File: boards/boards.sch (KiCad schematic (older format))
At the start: 3 parts

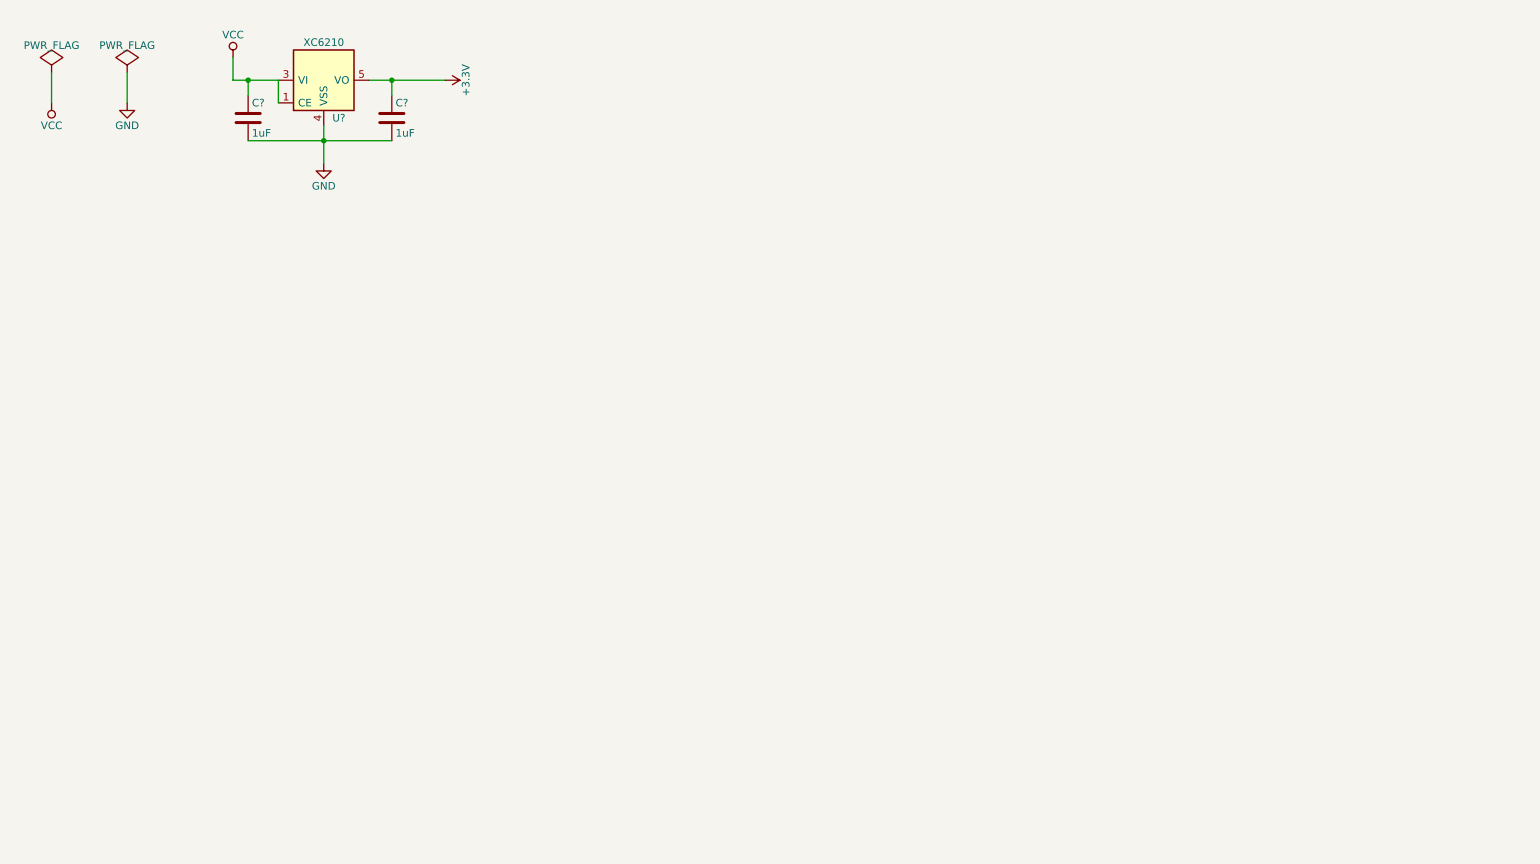
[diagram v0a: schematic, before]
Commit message: Schematics completed (rev 1). PCB layout started.
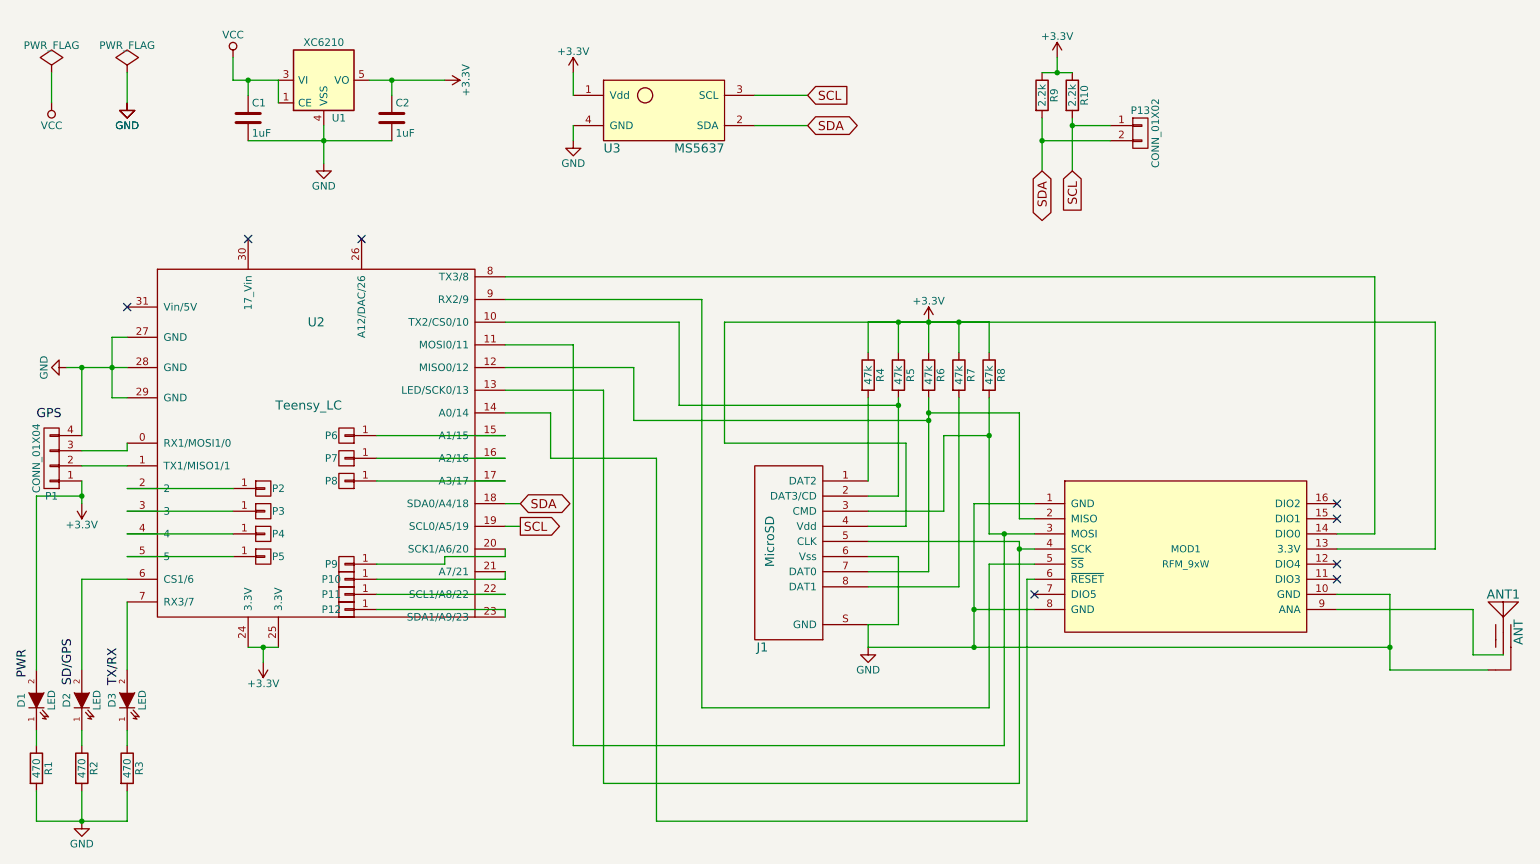
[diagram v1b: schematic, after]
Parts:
- added ANT1: ANT, Parts:ANT_50ohm, symbol ANT
- added D1: LED, william-parts:KPH-1608SGC, symbol LED
- added D2, D3: LED, william-parts:KingbrightKPTL-3216QBC-D-01, symbol LED
- added J1: MicroSD, Parts:DM3CS-SF, symbol MicroSD
- added MOD1: RFM_9xW, Parts:RFM9xW, symbol RFM_9xW
- added P1: CONN_01X04, william-parts:quadruple_pads, symbol CONN_01X04
- added P10, P11, P12, P2, P3, P4, P5, P6, P7, P8, P9: (no value), william-parts:single_pad, symbol CONN_01X01
- added P13: CONN_01X02, william-parts:double_pads, symbol CONN_01X02
- added R1, R2, R3: 470, Resistors_SMD.pretty:R_0805_HandSoldering, symbol R
- added R10, R9: 2.2k, Resistors_SMD.pretty:R_0805_HandSoldering, symbol R
- added R4, R5, R6, R7, R8: 47k, Resistors_SMD.pretty:R_0805_HandSoldering, symbol R
- added U2: Teensy_LC, william-parts:Teensy-LC, symbol Teensy_LC
- added U3: MS5637, Parts:MS5637, symbol MS5637
- C1, C2: renamed from C?; footprint (none) -> Capacitors_SMD.pretty:C_0805_HandSoldering
- U1: renamed from U?; footprint (none) -> TO_SOT_Packages_SMD.pretty:SOT-23-5
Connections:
- net +3V3: now also D1.2 (A), J1.4 (Vdd), MOD1.13 (3.3V), P1.1 (P1), R10.1, R4.1, R5.1, R6.1, R7.1, R8.1, R9.1, U2.24 (3.3V), U2.25 (3.3V), U3.1 (Vdd)
- net GND: now also ANT1.2, J1.6 (Vss), J1.S (GND), MOD1.1 (GND), MOD1.10 (GND), MOD1.8 (GND), P1.4 (P4), R1.2, R2.2, R3.2, U2.27 (GND), U2.28 (GND), U2.29 (GND), U3.4 (GND)
- new net: J1.1 (DAT2), R4.2
- new net: J1.2 (DAT3/CD), R5.2, U2.10 (TX2/CS0/10)
- new net: J1.3 (CMD), MOD1.3 (MOSI), R8.2, U2.11 (MOSI0/11)
- new net: J1.5 (CLK), MOD1.4 (SCK), U2.13 (LED/SCK0/13)
- new net: J1.7 (DAT0), MOD1.2 (MISO), R6.2, U2.12 (MISO0/12)
- new net: J1.8 (DAT1), R7.2
- new net: P1.3 (P3), U2.0 (RX1/MOSI1/0)
- new net: P1.2 (P2), U2.1 (TX1/MISO1/1)
- new net: MOD1.6 (~RESET), U2.14 (A0/14)
- new net: P6.1 (P1), U2.15 (A1/15)
- new net: P7.1 (P1), U2.16 (A2/16)
- new net: P8.1 (P1), U2.17 (A3/17)
- new net: P2.1 (P1), U2.2
- new net: P9.1 (P1), U2.20 (SCK1/A6/20)
- new net: P10.1 (P1), U2.21 (A7/21)
- new net: P11.1 (P1), U2.22 (SCL1/A8/22)
- new net: P12.1 (P1), U2.23 (SDA1/A9/23)
- new net: P3.1 (P1), U2.3
- new net: P4.1 (P1), U2.4
- new net: P5.1 (P1), U2.5
- new net: D2.2 (A), U2.6 (CS1/6)
- new net: D3.2 (A), U2.7 (RX3/7)
- new net: MOD1.14 (DIO0), U2.8 (TX3/8)
- new net: MOD1.5 (~SS), U2.9 (RX2/9)
- new net: ANT1.1, MOD1.9 (ANA)
- new net: D1.1 (K), R1.1
- new net: D2.1 (K), R2.1
- new net: D3.1 (K), R3.1
- new net SCL: P13.1 (P1), R10.2, U2.19 (SCL0/A5/19), U3.3 (SCL)
- new net SDA: P13.2 (P2), R9.2, U2.18 (SDA0/A4/18), U3.2 (SDA)
- no-connect marks 0 -> 8

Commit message: Changed to TO252 power reg. Continued trace connection.
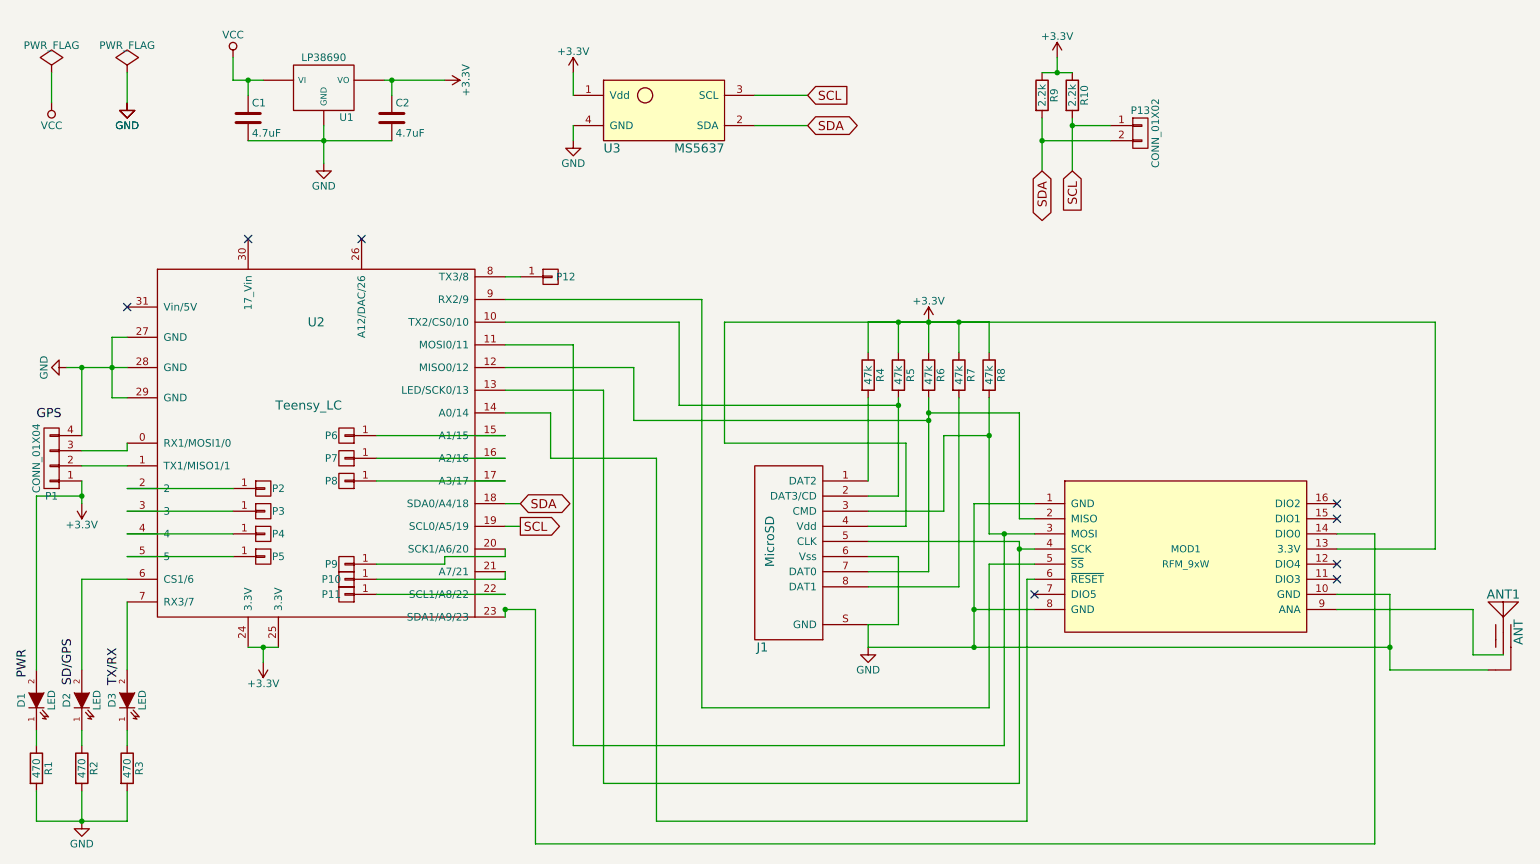
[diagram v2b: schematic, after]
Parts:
- removed U1: XC6210, TO_SOT_Packages_SMD.pretty:SOT-23-5, symbol XC6210
- added U1: LP38690, TO_SOT_Packages_SMD.pretty:TO-252-3Lead, symbol LP38690-RESCUE-boards
- C1, C2: value 1uF -> 4.7uF
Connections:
- net +3V3: now also U1.VO
- net GND: now also U1.GND
- net VCC: now also U1.VI
- net at U2.23 (SDA1/A9/23): now also MOD1.14 (DIO0); no longer P12.1 (P1)
- net at U2.8 (TX3/8): now also P12.1 (P1); no longer MOD1.14 (DIO0)
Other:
- moved on the sheet: P12
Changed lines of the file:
@@
 EESchema Schematic File Version 2
+LIBS:boards-rescue
 LIBS:power
 LIBS:device
@@
 $EndComp
 $Comp
-L XC6210 U1
-U 1 1 577AA2F4
-P 2650 950
-F 0 "U1" H 2750 700 50  0000 C CNN
-F 1 "XC6210" H 2650 1200 50  0000 C CNN
-F 2 "TO_SOT_Packages_SMD.pretty:SOT-23-5" H 2650 950 50  0001 C CNN
-F 3 "" H 2650 950 50  0000 C CNN
-	1    2650 950
-	1    0    0    -1
-$EndComp
-$Comp
 L C C1
 U 1 1 577AA342
 P 2150 1200
 F 0 "C1" H 2175 1300 50  0000 L CNN
-F 1 "1uF" H 2175 1100 50  0000 L CNN
+F 1 "4.7uF" H 2175 1100 50  0000 L CNN
 F 2 "Capacitors_SMD.pretty:C_0805_HandSoldering" H 2188 1050 50  0001 C CNN
 F 3 "" H 2150 1200 50  0000 C CNN
@@
 P 3100 1200
 F 0 "C2" H 3125 1300 50  0000 L CNN
-F 1 "1uF" H 3125 1100 50  0000 L CNN
+F 1 "4.7uF" H 3125 1100 50  0000 L CNN
 F 2 "Capacitors_SMD.pretty:C_0805_HandSoldering" H 3138 1050 50  0001 C CNN
 F 3 "" H 3100 1200 50  0000 C CNN
@@
 	2050 800  2050 950
 Wire Wire Line
-	2050 950  2350 950
-Wire Wire Line
-	2350 950  2350 1100
-Wire Wire Line
-	2950 950  3450 950
+	2050 950  2250 950
+Wire Wire Line
+	3050 950  3450 950
 Wire Wire Line
 	3100 950  3100 1050
@@
 Wire Wire Line
 	4150 3150 3850 3150
-Wire Wire Line
-	3850 2250 9600 2250
-Wire Wire Line
-	9600 2250 9600 3950
 Wire Wire Line
 	9600 3950 9350 3950
@@
 L CONN_01X01 P12
 U 1 1 577C5D22
-P 2800 4450
-F 0 "P12" H 2900 4450 50  0000 C CNN
-F 1 " " V 2900 4450 50  0000 C CNN
-F 2 "william-parts:single_pad" H 2800 4450 50  0001 C CNN
-F 3 "" H 2800 4450 50  0000 C CNN
-	1    2800 4450
-	-1   0    0    1
+P 4150 2250
+F 0 "P12" H 4250 2250 50  0000 C CNN
+F 1 " " V 4250 2250 50  0000 C CNN
+F 2 "william-parts:single_pad" H 4150 2250 50  0001 C CNN
+F 3 "" H 4150 2250 50  0000 C CNN
+	1    4150 2250
+	1    0    0    -1
 $EndComp
 $Comp
@@
 	3850 4500 3850 4450
 Wire Wire Line
-	3850 4450 3000 4450
+	3850 4450 4050 4450
 Wire Wire Line
 	3000 4350 3850 4350
@@
 Wire Wire Line
 	3000 3600 3850 3600
+Wire Wire Line
+	9600 3950 9600 6000
+Wire Wire Line
+	9600 6000 4050 6000
+Wire Wire Line
+	4050 6000 4050 4450
+Connection ~ 3850 4450
+Wire Wire Line
+	3850 2250 3950 2250
+$Comp
+L LP38690-RESCUE-boards U1
+U 1 1 5781818D
+P 2650 1000
+F 0 "U1" H 2800 804 50  0000 C CNN
+F 1 "LP38690" H 2650 1200 50  0000 C CNN
+F 2 "TO_SOT_Packages_SMD.pretty:TO-252-3Lead" H 2650 1000 50  0001 C CNN
+F 3 "" H 2650 1000 50  0000 C CNN
+	1    2650 1000
+	1    0    0    -1
+$EndComp
 $EndSCHEMATC

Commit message: Added power smoothing caps around board.
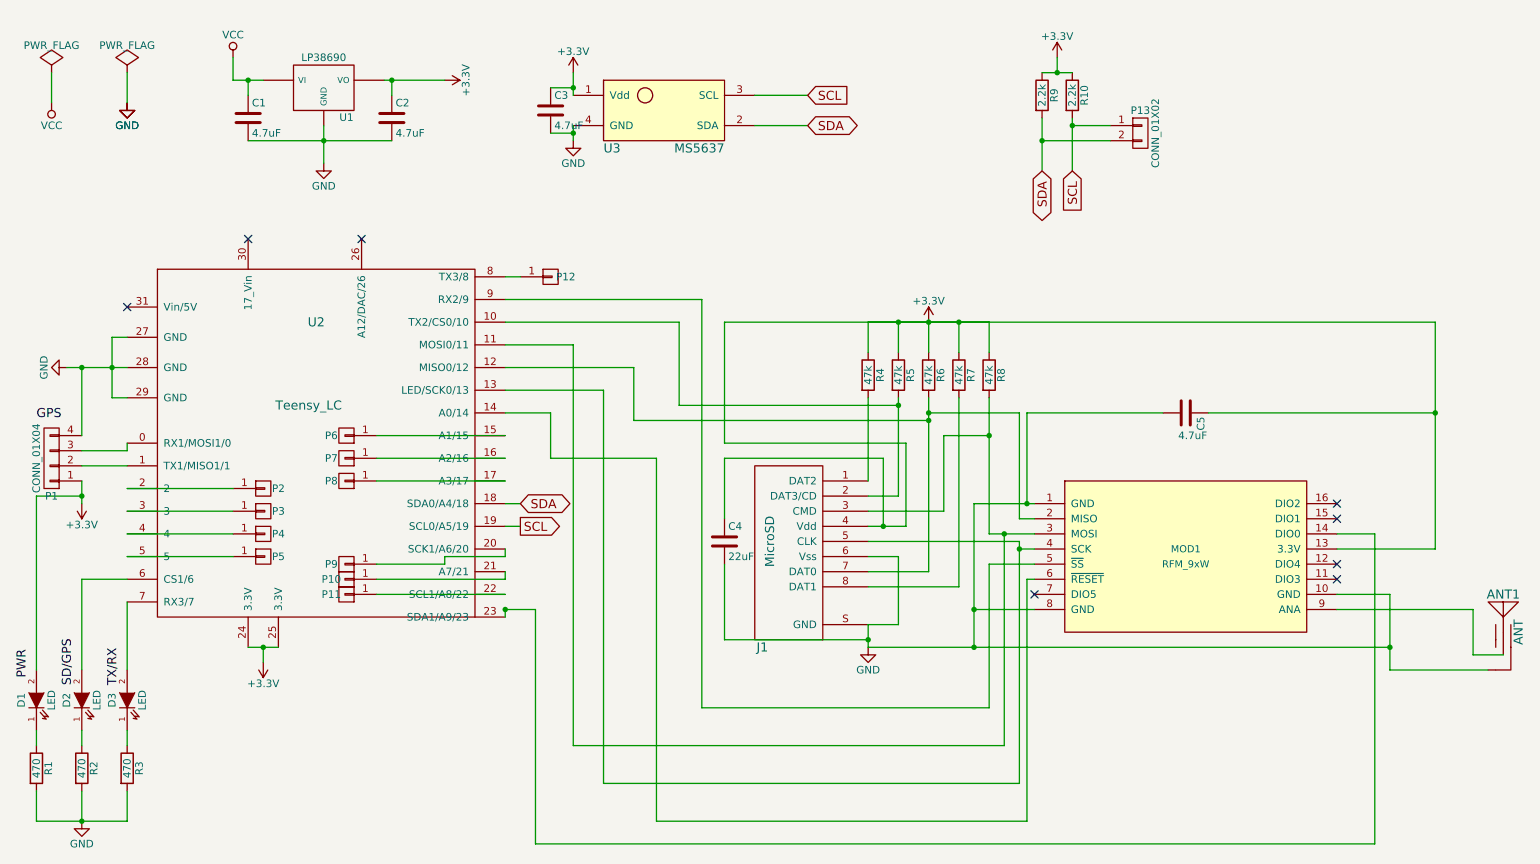
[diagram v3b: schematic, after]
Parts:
- added C3, C5: 4.7uF, Capacitors_SMD.pretty:C_0805_HandSoldering, symbol C
- added C4: 22uF, Capacitors_SMD.pretty:C_1206_HandSoldering, symbol C
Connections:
- net +3V3: now also C3.1, C4.1, C5.1
- net GND: now also C3.2, C4.2, C5.2

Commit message: Completed design. Not yet checked/verified.
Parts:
- added P14, P15, P16, P17, P18, P19, P20, P21, P22: CONN_01X01, william-parts:single_pad, symbol CONN_01X01
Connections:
- net +3V3: now also P18.1 (P1), P19.1 (P1), P20.1 (P1), P21.1 (P1)
- net GND: now also P14.1 (P1), P15.1 (P1), P16.1 (P1), P17.1 (P1)
- net VCC: now also P22.1 (P1)
